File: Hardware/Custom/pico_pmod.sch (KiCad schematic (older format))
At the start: 25 parts

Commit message: add capasitor details
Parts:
- C? (x4): footprint (none) -> Capacitor_SMD:C_0603_1608Metric
- C? (x7): value C -> 100n; footprint (none) -> Capacitor_SMD:C_0603_1608Metric
- C?: value C -> 100n
- J1, J2, J3: renamed from J?; footprint (none) -> Connector_PinHeader_2.54mm:PinHeader_2x06_P2.54mm_Vertical
- J4: renamed from J?; footprint (none) -> Connector_USB:USB_C_Receptacle_GCT_USB4085
- gave numbers to parts that had none: 1
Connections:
- net GPIO_0: now also J1.2 (Pin_2)
- net GPIO_1: now also J1.1 (Pin_1)
- net GPIO_2: now also J1.4 (Pin_4)
- net GPIO_3: now also J1.3 (Pin_3)
- net GPIO_4: now also J1.6 (Pin_6)
- net GPIO_5: now also J1.5 (Pin_5)
- net GPIO_6: now also J1.8 (Pin_8)
- net GPIO_7: now also J1.7 (Pin_7)
- net SWCLK: now reaches U1.24 (SWCLK)
- net SWDIO: now reaches U1.25 (SWD)
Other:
- note added: "DEBUG"
- moved on the sheet: J2, J3

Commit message: initial functional PCB layout
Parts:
- R3, R4: renamed from R?; footprint (none) -> Resistor_SMD:R_0603_1608Metric
- U1: footprint RP2040_minimal:RP2040-QFN-56 -> RaspberryPi:RP2040-QFN-56
- gave numbers to parts that had none: 18

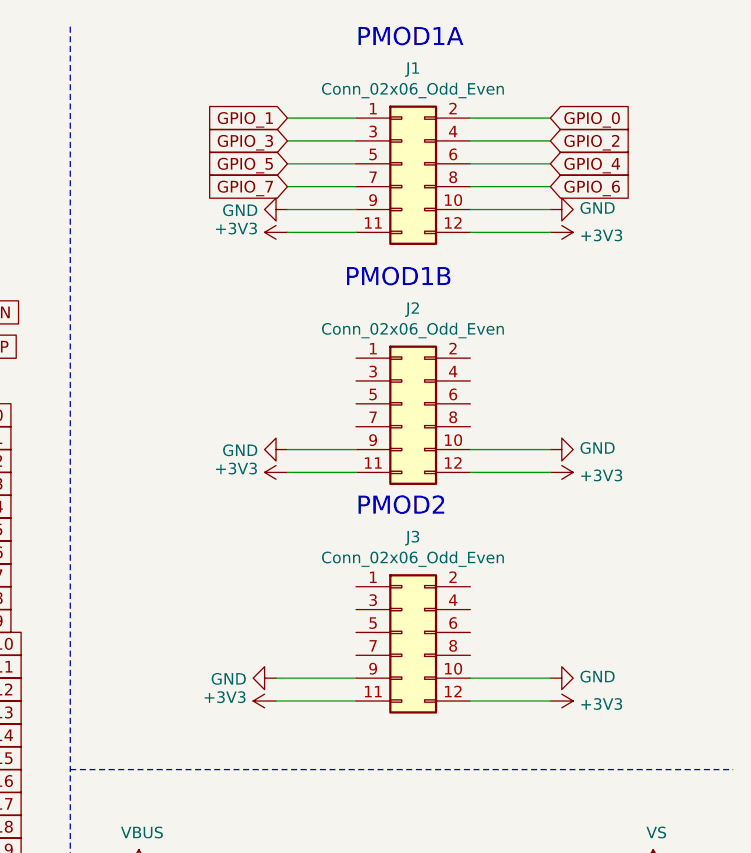
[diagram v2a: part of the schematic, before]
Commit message: Add the switchs footprints and put on PCB
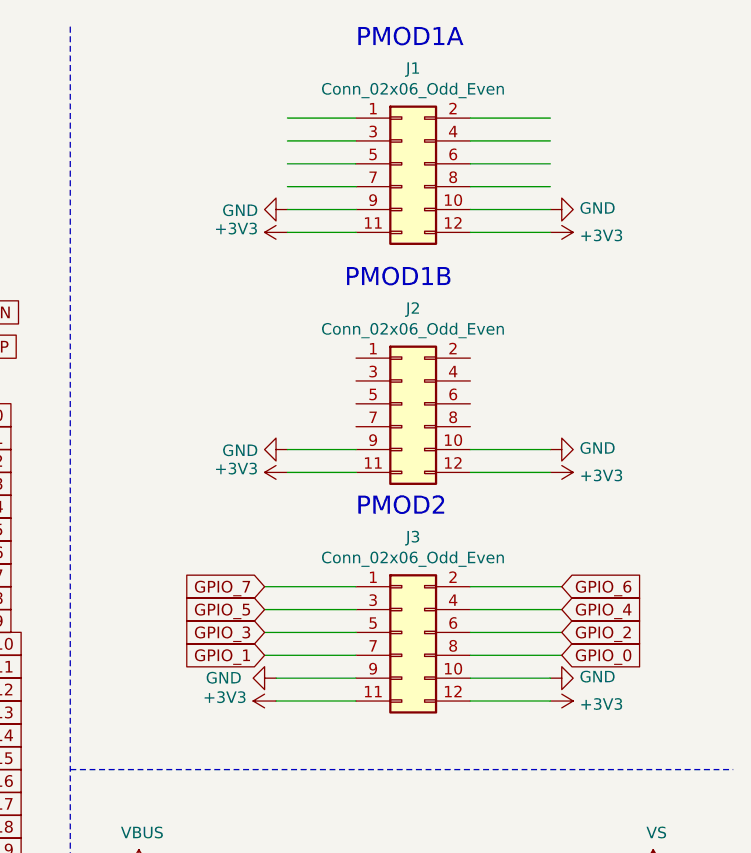
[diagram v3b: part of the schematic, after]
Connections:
- wire segments 131 -> 139
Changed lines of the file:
@@
 P 9200 3350
 F 0 "#PWR0104" H 9200 3100 50  0001 C CNN
-F 1 "GND" V 9205 3222 50  0000 R CNN
+F 1 "GND" V 9200 3200 50  0000 R CNN
 F 2 "" H 9200 3350 50  0001 C CNN
 F 3 "" H 9200 3350 50  0001 C CNN
@@
 Wire Wire Line
 	5850 1400 5750 1400
-Text GLabel 10400 900  2    51   Input ~ 0
+Text GLabel 10450 2950 2    51   Input ~ 0
+GPIO_6
+Text GLabel 9150 2950 0    51   Input ~ 0
+GPIO_7
+Text GLabel 10450 3050 2    51   Input ~ 0
+GPIO_4
+Text GLabel 9150 3050 0    51   Input ~ 0
+GPIO_5
+Text GLabel 10450 3150 2    51   Input ~ 0
+GPIO_2
+Text GLabel 9150 3150 0    51   Input ~ 0
+GPIO_3
+Text GLabel 10450 3250 2    51   Input ~ 0
 GPIO_0
-Text GLabel 9250 900  0    51   Input ~ 0
+Text GLabel 9150 3250 0    51   Input ~ 0
 GPIO_1
-Text GLabel 10400 1000 2    51   Input ~ 0
-GPIO_2
-Text GLabel 9250 1000 0    51   Input ~ 0
-GPIO_3
-Text GLabel 10400 1100 2    51   Input ~ 0
-GPIO_4
-Text GLabel 9250 1100 0    51   Input ~ 0
-GPIO_5
-Text GLabel 10400 1200 2    51   Input ~ 0
-GPIO_6
-Text GLabel 9250 1200 0    51   Input ~ 0
-GPIO_7
 Wire Wire Line
 	9250 900  9550 900
@@
 	1    0    0    -1
 $EndComp
+Wire Wire Line
+	9150 3250 9550 3250
+Wire Wire Line
+	9550 3150 9150 3150
+Wire Wire Line
+	9150 3050 9550 3050
+Wire Wire Line
+	9550 2950 9150 2950
+Wire Wire Line
+	10050 3250 10450 3250
+Wire Wire Line
+	10050 3150 10450 3150
+Wire Wire Line
+	10050 3050 10450 3050
+Wire Wire Line
+	10050 2950 10450 2950
 $EndSCHEMATC

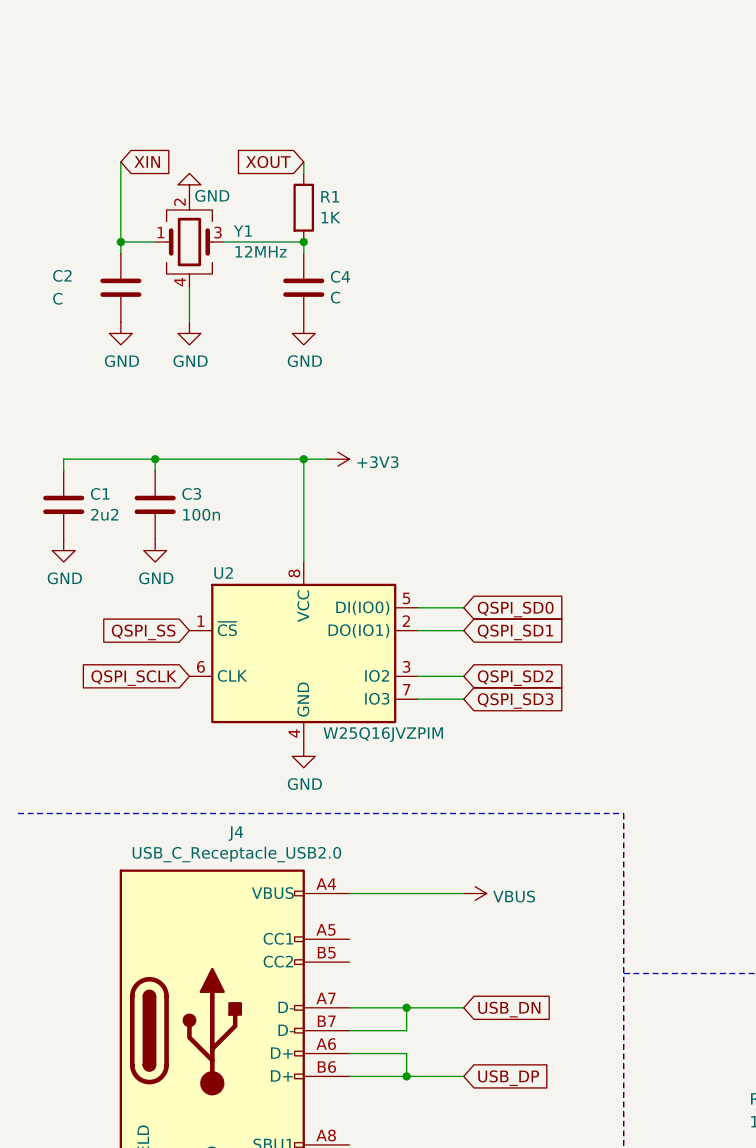
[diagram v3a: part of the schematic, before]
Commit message: Add usb CC 1 and 2 resistors
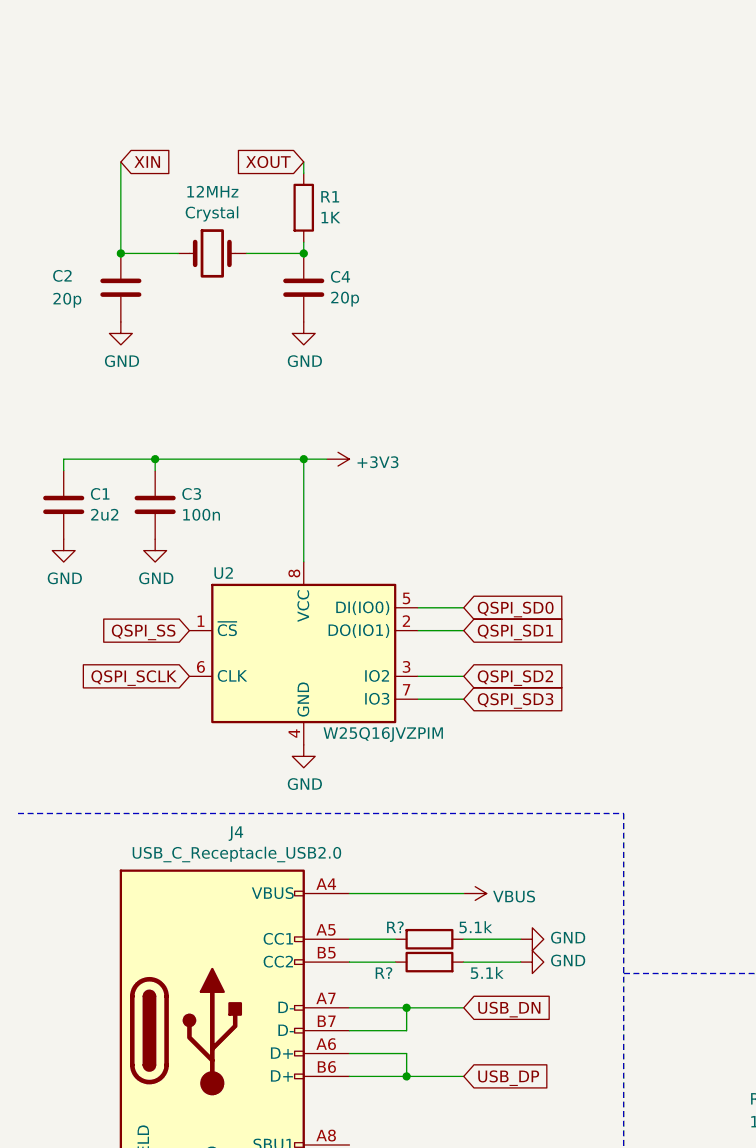
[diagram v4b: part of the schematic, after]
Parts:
- removed Y1: 12MHz, symbol Device:Crystal_GND24
- added 12MHz: Crystal, RaspberryPi:Crystal_SMD_HC49-US, symbol Device:Crystal
- added R? (x2): 5.1k, symbol Device:R
- C2, C4: value C -> 20p
- C9: footprint (none) -> Capacitor_SMD:C_0603_1608Metric
- J4: footprint Connector_USB:USB_C_Receptacle_GCT_USB4085 -> Connector_USB:USB_C_Receptacle_Amphenol_12401610E4-2A_CircularHoles
- R2: footprint (none) -> Resistor_SMD:R_0603_1608Metric
- SW1, SW2: footprint (none) -> Button_Switch_THT:SW_PUSH_6mm_H4.3mm
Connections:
- wire segments 139 -> 141
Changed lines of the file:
@@
 F 0 "SW1" V 3850 7685 50  0000 C CNN
 F 1 "SW_Push" V 3750 7700 50  0000 C CNN
-F 2 "" H 3850 7600 50  0001 C CNN
+F 2 "Button_Switch_THT:SW_PUSH_6mm_H4.3mm" H 3850 7600 50  0001 C CNN
 F 3 "~" H 3850 7600 50  0001 C CNN
 	1    3850 7400
@@
 F 0 "SW2" H 5700 7485 50  0000 C CNN
 F 1 "SW_Push" H 5700 7394 50  0000 C CNN
-F 2 "" H 5700 7400 50  0001 C CNN
+F 2 "Button_Switch_THT:SW_PUSH_6mm_H4.3mm" H 5700 7400 50  0001 C CNN
 F 3 "~" H 5700 7400 50  0001 C CNN
 	1    5700 7200
@@
 F 0 "R2" H 3650 6950 50  0000 L CNN
 F 1 "1K" H 3650 6850 50  0000 L CNN
-F 2 "" V 3780 6900 50  0001 C CNN
+F 2 "Resistor_SMD:R_0603_1608Metric" V 3780 6900 50  0001 C CNN
 F 3 "~" H 3850 6900 50  0001 C CNN
 	1    3850 6900
@@
 F 0 "J4" H 1407 7417 50  0000 C CNN
 F 1 "USB_C_Receptacle_USB2.0" H 1407 7326 50  0000 C CNN
-F 2 "Connector_USB:USB_C_Receptacle_GCT_USB4085" H 1450 6550 50  0001 C CNN
+F 2 "Connector_USB:USB_C_Receptacle_Amphenol_12401610E4-2A_CircularHoles" H 1450 6550 50  0001 C CNN
 F 3 "https://www.usb.org/sites/default/files/documents/usb_type-c.zip" H 1450 6550 50  0001 C CNN
 	1    1300 6550
@@
 	5200 5500 5200 5650
 $Comp
-L Device:Crystal_GND24 Y1
-U 1 1 60FE57C7
-P 1200 3100
-F 0 "Y1" H 1394 3146 50  0000 L CNN
-F 1 "12MHz" H 1394 3055 50  0000 L CNN
-F 2 "" H 1200 3100 50  0001 C CNN
-F 3 "~" H 1200 3100 50  0001 C CNN
-	1    1200 3100
-	1    0    0    -1
-$EndComp
-$Comp
 L power:GND #PWR0123
 U 1 1 60FE8947
@@
 $EndComp
 $Comp
-L power:GND #PWR0125
-U 1 1 60FE966C
-P 1200 3450
-F 0 "#PWR0125" H 1200 3200 50  0001 C CNN
-F 1 "GND" H 1205 3277 50  0000 C CNN
-F 2 "" H 1200 3450 50  0001 C CNN
-F 3 "" H 1200 3450 50  0001 C CNN
-	1    1200 3450
-	1    0    0    -1
-$EndComp
-$Comp
 L Device:C C2
 U 1 1 60FE9B7C
 P 900 3300
 F 0 "C2" H 600 3350 50  0000 L CNN
-F 1 "C" H 600 3250 50  0000 L CNN
+F 1 "20p" H 600 3250 50  0000 L CNN
 F 2 "Capacitor_SMD:C_0603_1608Metric" H 938 3150 50  0001 C CNN
 F 3 "~" H 900 3300 50  0001 C CNN
@@
 P 1700 3300
 F 0 "C4" H 1815 3346 50  0000 L CNN
-F 1 "C" H 1815 3255 50  0000 L CNN
+F 1 "20p" H 1815 3255 50  0000 L CNN
 F 2 "Capacitor_SMD:C_0603_1608Metric" H 1738 3150 50  0001 C CNN
 F 3 "~" H 1700 3300 50  0001 C CNN
@@
 	1    0    0    -1
 $EndComp
-Wire Wire Line
-	1200 3450 1200 3300
-Wire Wire Line
-	1050 3100 900  3100
-Wire Wire Line
-	900  3100 900  3150
-Wire Wire Line
-	1350 3100 1700 3100
 Wire Wire Line
 	1700 3100 1700 3150
@@
 	1    0    0    -1
 $EndComp
-Connection ~ 1700 3100
 Text GLabel 900  2750 2    51   Input ~ 0
 XIN
@@
 Wire Wire Line
 	1700 2750 1700 2800
-Wire Wire Line
-	900  3100 900  2750
-Connection ~ 900  3100
-$Comp
-L power:GND #PWR0126
-U 1 1 60FFB985
-P 1200 2900
-F 0 "#PWR0126" H 1200 2650 50  0001 C CNN
-F 1 "GND" H 1100 2900 50  0000 C CNN
-F 2 "" H 1200 2900 50  0001 C CNN
-F 3 "" H 1200 2900 50  0001 C CNN
-	1    1200 2900
-	-1   0    0    1
-$EndComp
 Text GLabel 4250 3600 0    51   Input ~ 0
 XIN
@@
 F 0 "C9" H 6500 900 50  0000 L CNN
 F 1 "100n" H 6500 700 50  0000 L CNN
-F 2 "" H 6488 650 50  0001 C CNN
+F 2 "Capacitor_SMD:C_0603_1608Metric" H 6488 650 50  0001 C CNN
 F 3 "~" H 6450 800 50  0001 C CNN
 	1    6450 800
@@
 Wire Wire Line
 	10050 2950 10450 2950
+$Comp
+L Device:Crystal 12MHz
+U 1 1 60F9336B
+P 1300 3150
+F 0 "12MHz" H 1300 3418 50  0000 C CNN
+F 1 "Crystal" H 1300 3327 50  0000 C CNN
+F 2 "RaspberryPi:Crystal_SMD_HC49-US" H 1300 3150 50  0001 C CNN
+F 3 "~" H 1300 3150 50  0001 C CNN
+F 4 "ABLS-12.000MHZ-B4-T" H 1300 3150 50  0001 C CNN "Part"
+	1    1300 3150
+	1    0    0    -1
+$EndComp
+Wire Wire Line
+	900  2750 900  3150
+Wire Wire Line
+	1150 3150 900  3150
+Connection ~ 900  3150
+Wire Wire Line
+	1450 3150 1700 3150
+Connection ~ 1700 3150
+$Comp
+L Device:R R?
+U 1 1 60FC2CF3
+P 2250 6150
+F 0 "R?" V 2200 6000 50  0000 C CNN
+F 1 "5.1k" V 2200 6350 50  0000 C CNN
+F 2 "" V 2180 6150 50  0001 C CNN
+F 3 "~" H 2250 6150 50  0001 C CNN
+	1    2250 6150
+	0    1    1    0
+$EndComp
+$Comp
+L Device:R R?
+U 1 1 60FC35B9
+P 2250 6250
+F 0 "R?" V 2200 6450 50  0000 C CNN
+F 1 "5.1k" V 2200 6000 50  0000 C CNN
+F 2 "" V 2180 6250 50  0001 C CNN
+F 3 "~" H 2250 6250 50  0001 C CNN
+	1    2250 6250
+	0    -1   -1   0
+$EndComp
+Wire Wire Line
+	1900 6150 2100 6150
+Wire Wire Line
+	2100 6250 1900 6250
+$Comp
+L power:GND #PWR?
+U 1 1 60FD373C
+P 2650 6150
+F 0 "#PWR?" H 2650 5900 50  0001 C CNN
+F 1 "GND" V 2655 6022 50  0000 R CNN
+F 2 "" H 2650 6150 50  0001 C CNN
+F 3 "" H 2650 6150 50  0001 C CNN
+	1    2650 6150
+	0    -1   -1   0
+$EndComp
+$Comp
+L power:GND #PWR?
+U 1 1 60FD3DFE
+P 2650 6250
+F 0 "#PWR?" H 2650 6000 50  0001 C CNN
+F 1 "GND" V 2655 6122 50  0000 R CNN
+F 2 "" H 2650 6250 50  0001 C CNN
+F 3 "" H 2650 6250 50  0001 C CNN
+	1    2650 6250
+	0    -1   -1   0
+$EndComp
+Wire Wire Line
+	2650 6250 2400 6250
+Wire Wire Line
+	2650 6150 2400 6150
 $EndSCHEMATC

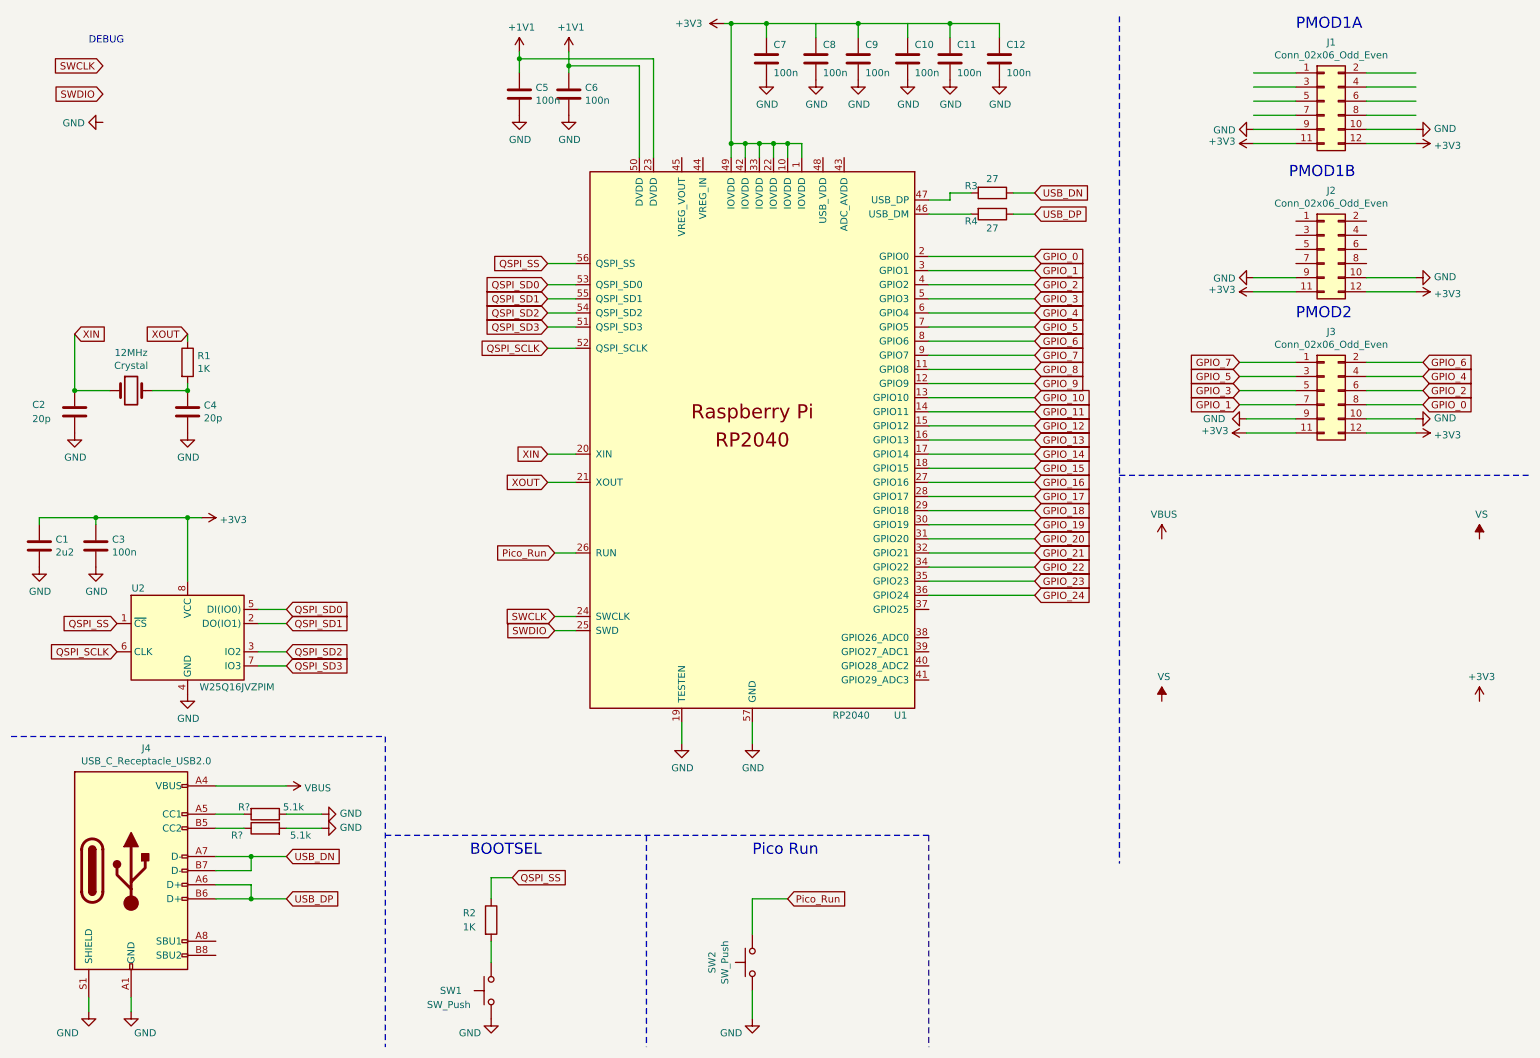
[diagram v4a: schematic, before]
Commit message: Add power supply and spi memory
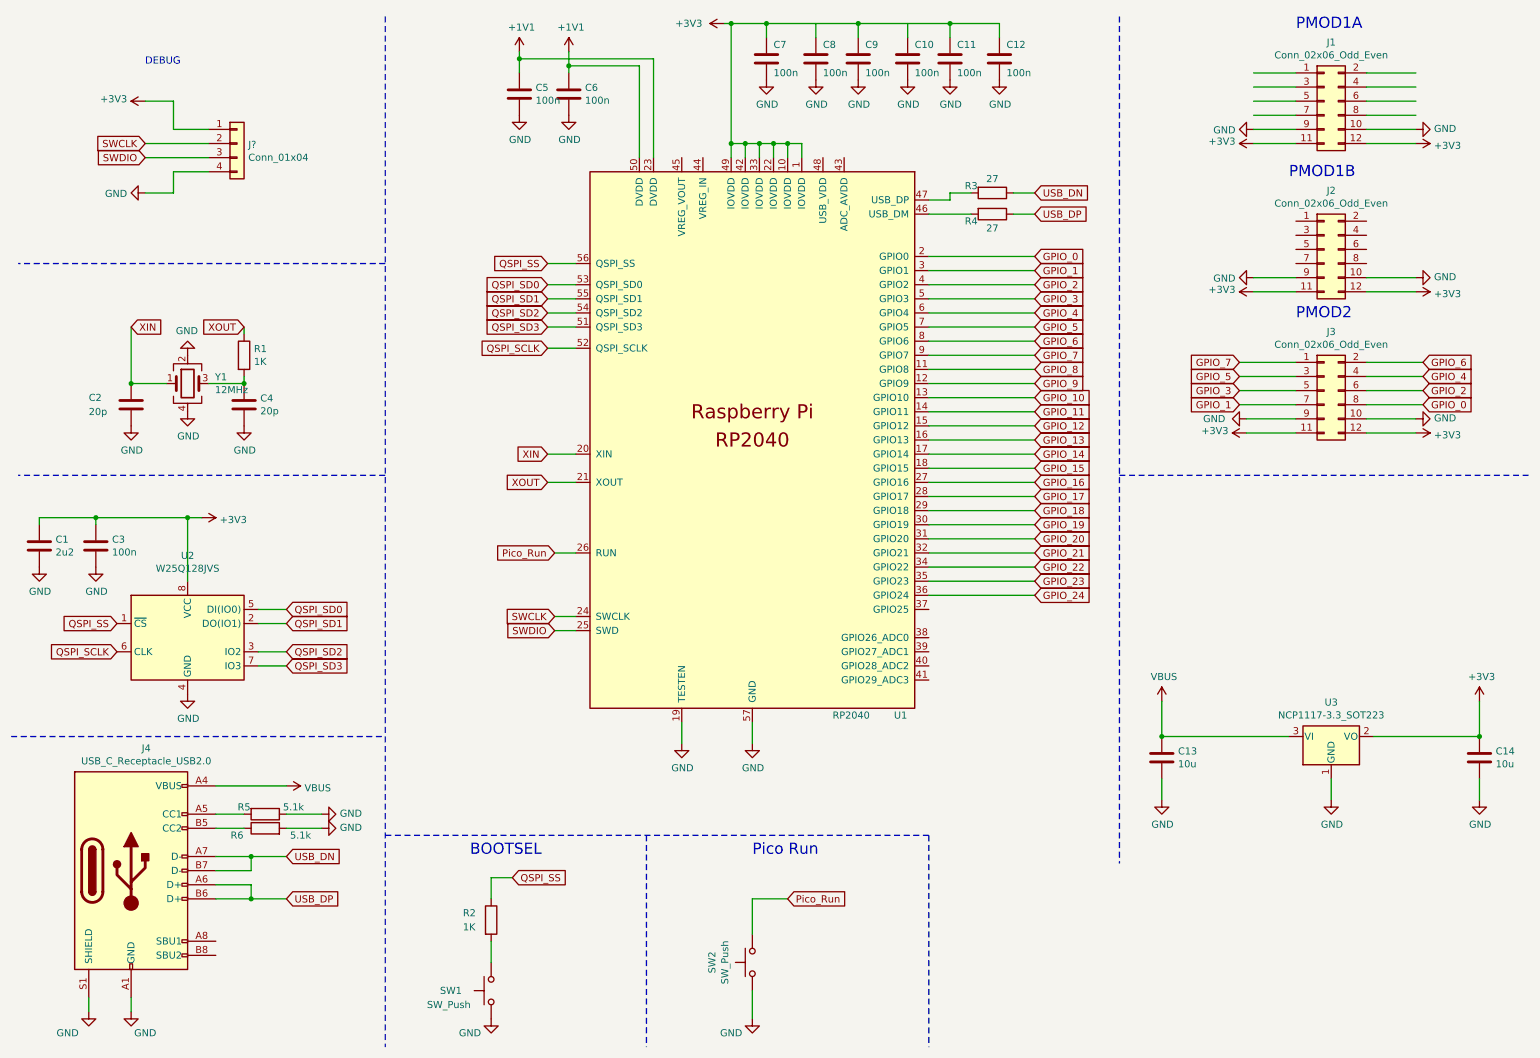
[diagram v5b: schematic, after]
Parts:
- removed 12MHz: Crystal, RaspberryPi:Crystal_SMD_HC49-US, symbol Device:Crystal
- removed U2: W25Q16JVZPIM, symbol Memory_Flash:W25Q32JVSS
- added C13, C14: 10u, Capacitor_SMD:C_0603_1608Metric, symbol Device:C
- added J?: Conn_01x04, symbol Connector_Generic:Conn_01x04
- added U2: W25Q128JVS, Package_SO:SOIC-8_5.23x5.23mm_P1.27mm, symbol Memory_Flash:W25Q128JVS
- added U3: NCP1117-3.3_SOT223, Package_TO_SOT_SMD:SOT-223-3_TabPin2, symbol Regulator_Linear:NCP1117-3.3_SOT223
- added Y1: 12MHz, Crystal:Crystal_SMD_SeikoEpson_FA238-4Pin_3.2x2.5mm, symbol Device:Crystal_GND24
- R1: footprint (none) -> Resistor_SMD:R_0603_1608Metric
- R5, R6: renamed from R?; footprint (none) -> Resistor_SMD:R_0603_1608Metric
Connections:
- net labels removed: VS
- wire segments 141 -> 156
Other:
- moved on the sheet: C2, C4, R1
